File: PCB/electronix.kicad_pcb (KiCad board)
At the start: 2 copper layers, 83.6 x 83.2 mm, 98 parts, among them IC1 ICM-20602, IC2 AP9101CK6-ANTRG1, IC3 DRV8210DRLR, IC4 DRV8210DRLR, J1 USB-C 6pin, J2 PRG, M1 N20 motor, M2 N20 motor, Q1 UMH3N FHA, Q2 757-SSM6N7002KFULF, Q3 757-SSM6N7002KFULF, Q4 Phototransistor, Q5 Phototransistor, Q6 757-SSM6N7002KFULF, Q7 Phototransistor, Q8 Phototransistor, SW1 SW_DIP_x01, SW2 RESET, SW3 START, U1 MCP73213-A6SI/MF, U2 ESP32-WROOM-32, U3 LMR51420YDDRCR

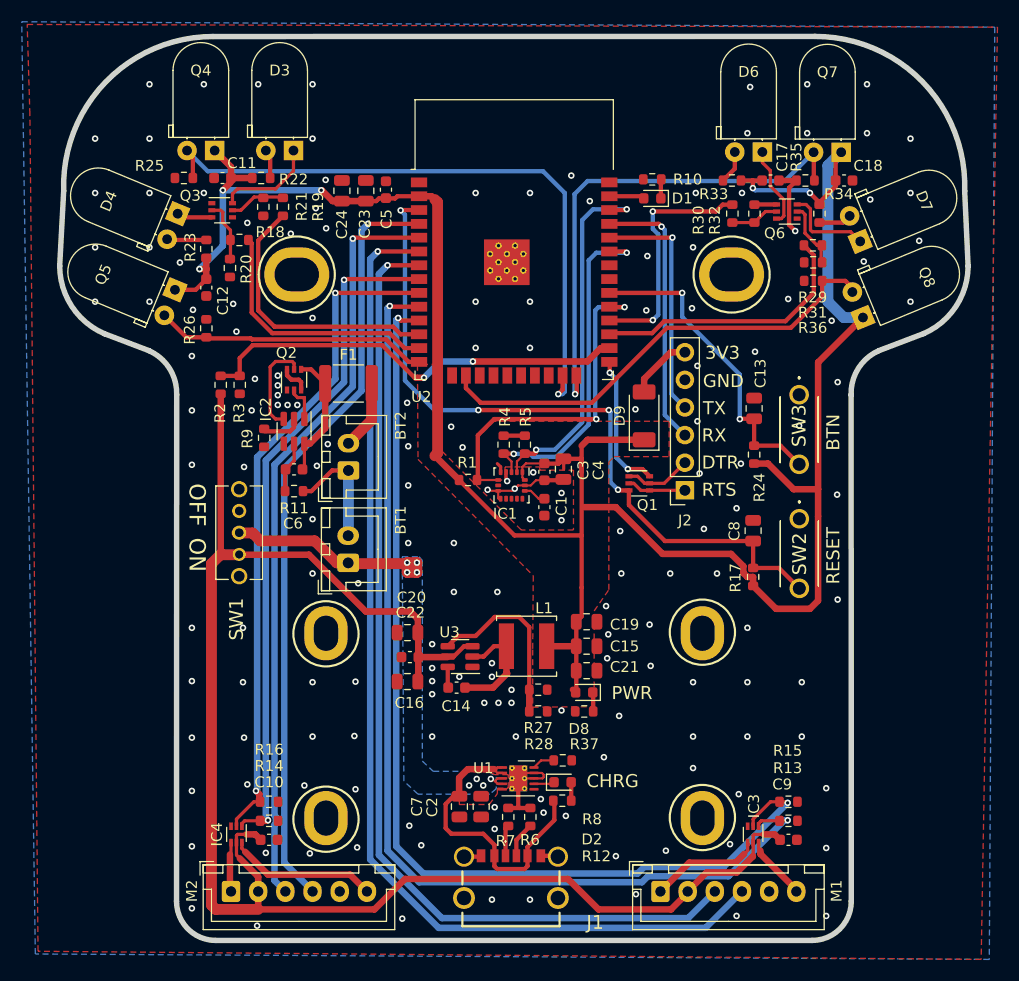
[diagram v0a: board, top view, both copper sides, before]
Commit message: EMI Hardening
Rerouted back layer tracks whereever possible to create a continuous ground plane
Added local vias to all gnd pins
Added via stitching to overhanging areas from the front
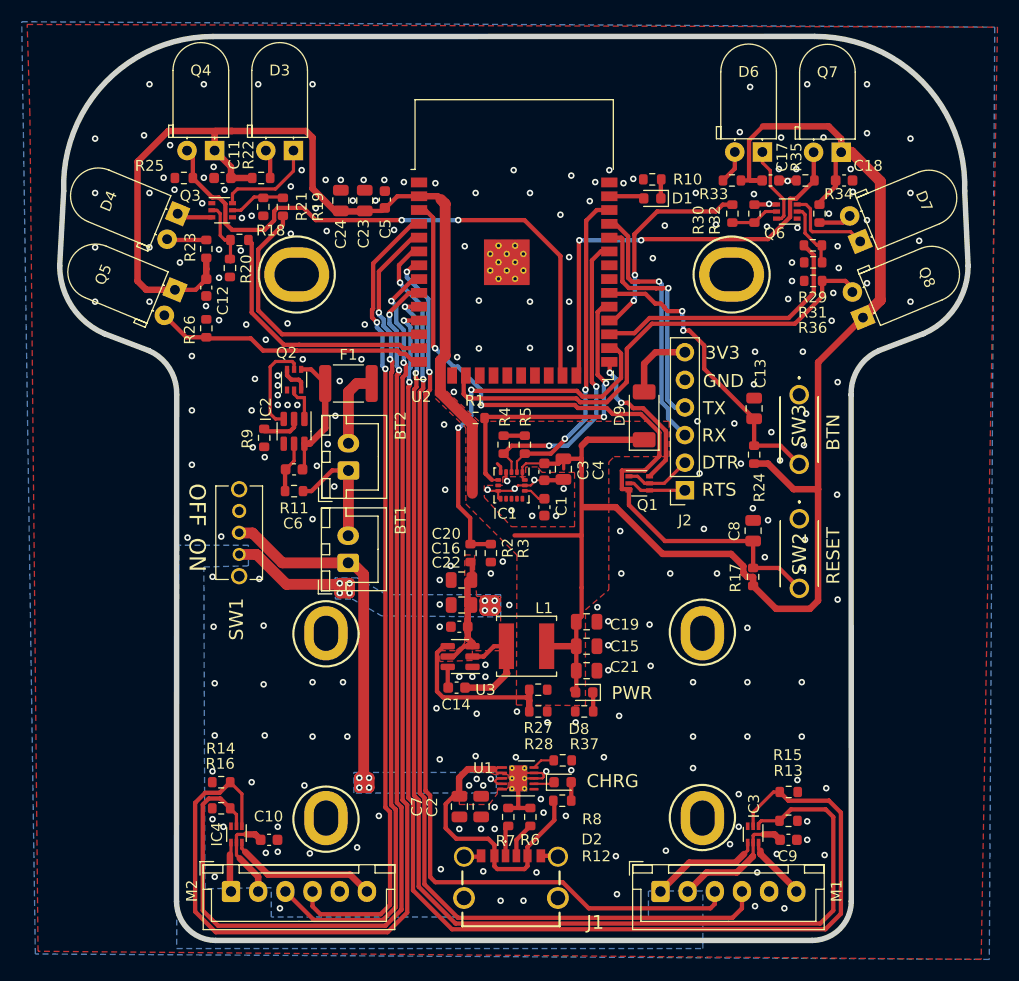
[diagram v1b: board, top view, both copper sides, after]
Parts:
- moved R3 27.8 mm to (128.9, 109.6)
- moved R2 27.7 mm to (127.0, 109.6)
- moved C16 8.62 mm to (126.2, 114.4)
- moved C20 6.94 mm to (126.2, 112.1)
- moved R1 5.74 mm to (127.5, 97.2)
- moved R14 5.65 mm to (104.1, 130.7), turned to 180 degrees
- moved C22 5.33 mm to (126.0, 116.4)
- moved R16 4.44 mm to (104.1, 133.1), turned to 180 degrees
- moved C23 0.91 mm to (117.3, 77.2)
- moved C24 0.91 mm to (115.1, 77.2)
- moved C5 0.91 mm to (119.2, 77.1)
- moved R15 0.90 mm to (156.3, 131.6)
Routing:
- net VCC: track 148.2 -> 49.2 mm, vias 0 -> 8
- net /M2in1: track 62.5 -> 99.5 mm
- net /M2in2: track 61.1 -> 93.2 mm
- net +3V3: track 218.2 -> 242.9 mm, vias 5 -> 0
- net /M1in2: track 94.9 -> 116.0 mm
- net /M1in1: track 96.3 -> 112.0 mm
- net +BATT: track 21.8 -> 36.9 mm
- net /M2c2: track 69.7 -> 76.0 mm, vias 1 -> 2
- net /prox_out_fr: track 46.4 -> 40.0 mm, vias 1 -> 2
- net /prox_out_fl: track 60.0 -> 53.8 mm, vias 1 -> 2
- net /M1c2: track 91.8 -> 86.4 mm, vias 1 -> 2
- net /M1c1: track 98.2 -> 92.9 mm, vias 1 -> 2
- net GND: track 30.2 -> 25.0 mm, vias 170 -> 245
- net /v_sense: track 40.2 -> 35.2 mm
- net /M2c1: track 70.3 -> 74.6 mm, vias 1 -> 2
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- added copper zone on B.Cu, net VCC
- added copper zone on F.Cu, net VCC

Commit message: Add power source switching Add Mouser PN to parts to enable BOM generation Moved PWR indicator to side of board
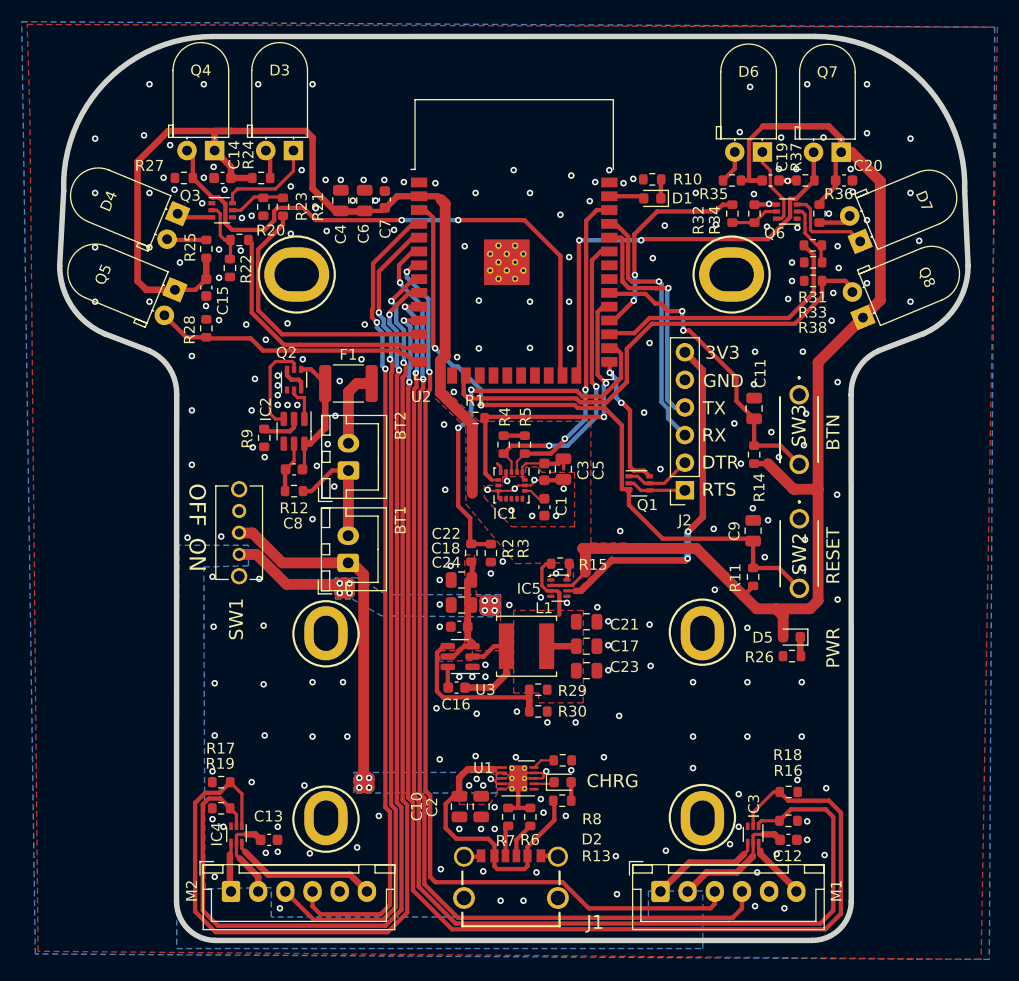
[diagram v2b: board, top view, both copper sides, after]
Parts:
- removed D8: LED, LED_SMD:LED_0603_1608Metric
- removed D9: D, Diode_SMD:D_SOD-128
- removed the R37 at (137.5, 124.2)
- added D5: LED, LED_SMD:LED_0603_1608Metric, F.Cu at (156.6, 117.4)
- added IC5: LM66200DRLR, Package_TO_SOT_SMD:SOT-583-8, F.Cu at (135.2, 112.8)
- added R15: 10k, Resistor_SMD:R_0603_1608Metric, F.Cu at (135.3, 110.6)
- added R26: 330R, Resistor_SMD:R_0603_1608Metric, F.Cu at (156.6, 119.1)
- moved R2 0.08 mm to (127.1, 109.6)
- renumbered C7 to C10, C13 to C11, C9 to C12, C10 to C13, C11 to C14, C12 to C15, C14 to C16, C15 to C17, C16 to C18, C17 to C19, C18 to C20, C19 to C21, C20 to C22, C21 to C23, C22 to C24, C24 to C4, C4 to C5, C23 to C6, C5 to C7, C6 to C8, C8 to C9, R17 to R11, R11 to R12, R12 to R13, R24 to R14, R13 to R16, R14 to R17, R15 to R18, R16 to R19, R18 to R20, R19 to R21, R20 to R22, R21 to R23, R22 to R24, R23 to R25, R25 to R27, R26 to R28, R27 to R29, R28 to R30, R29 to R31, R30 to R32, R31 to R33, R32 to R34, R33 to R35, R34 to R36, R35 to R37, R36 to R38
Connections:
- C17 pad 1: +3V3 -> /3V3_SW
- C21 pad 1: +3V3 -> /3V3_SW
- C23 pad 1: +3V3 -> /3V3_SW
- J2 pad 6: Net-(D9-A) -> /3V3_PRG
- L1 pad 2: +3V3 -> /3V3_SW
- R29 pad 1: +3V3 -> /3V3_SW
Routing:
- net +3V3: track 242.9 -> 209.8 mm
- net /3V3_PRG: track 0.00 -> 32.6 mm, vias 0 -> 2
- net /3V3_SW: track 0.00 -> 9.25 mm
- net Net-(D9-A): track 6.78 -> 0.00 mm
- net /EN: track 68.8 -> 62.8 mm
- net Net-(D5-K): track 0.00 -> 1.71 mm
- net Net-(D8-K): track 1.71 -> 0.00 mm
- net Net-(IC5-ST): track 0.00 -> 1.58 mm
- net /IO0: track 14.2 -> 12.7 mm
- net GND: vias 245 -> 247
- added copper zone on F.Cu, net /3V3_SW

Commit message: Finishing touches shorten ground plane cuts fillet polygon pours add test points and PSU bringup jumper differentiate capacitor footprints by silkscreen
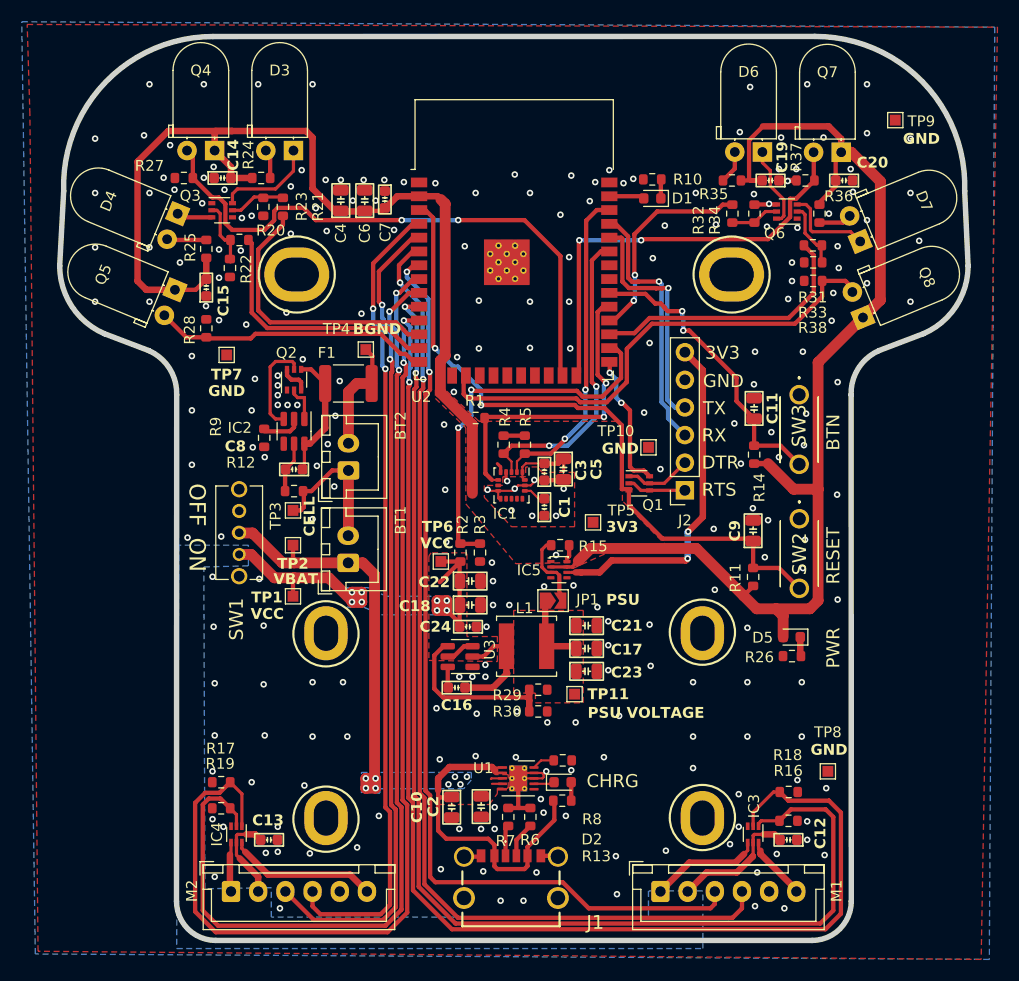
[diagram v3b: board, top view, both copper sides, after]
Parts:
- added JP1: SolderJumper_2_Open, Jumper:SolderJumper-2_P1.3mm_Open_TrianglePad1.0x1.5mm, F.Cu at (134.6, 114.0)
- added TP1: TestPoint, TestPoint:TestPoint_Pad_1.0x1.0mm, F.Cu at (110.7, 113.6)
- added TP10: TestPoint, TestPoint:TestPoint_Pad_1.0x1.0mm, F.Cu at (143.4, 99.9)
- added TP11: TestPoint, TestPoint:TestPoint_Pad_1.0x1.0mm, F.Cu at (136.6, 122.6)
- added TP2: TestPoint, TestPoint:TestPoint_Pad_1.0x1.0mm, F.Cu at (110.7, 108.9)
- added TP3: TestPoint, TestPoint:TestPoint_Pad_1.0x1.0mm, F.Cu at (110.7, 105.7)
- added TP4: TestPoint, TestPoint:TestPoint_Pad_1.0x1.0mm, F.Cu at (117.4, 90.9)
- added TP5: TestPoint, TestPoint:TestPoint_Pad_1.0x1.0mm, F.Cu at (138.3, 106.8)
- added TP6: TestPoint, TestPoint:TestPoint_Pad_1.0x1.0mm, F.Cu at (124.3, 110.4)
- added TP7: TestPoint, TestPoint:TestPoint_Pad_1.0x1.0mm, F.Cu at (104.6, 91.4)
- added TP8: TestPoint, TestPoint:TestPoint_Pad_1.0x1.0mm, F.Cu at (159.9, 129.7)
- added TP9: TestPoint, TestPoint:TestPoint_Pad_1.0x1.0mm, F.Cu at (166.1, 69.8)
- C1, C12, C13, C14, C15, C16, C19, C20, C3, C7, C8: footprint Capacitor_SMD:C_0603_1608Metric -> Custom_parts:C_0603_1608Metric
- C10, C11, C17, C18, C2, C21, C22, C23, C4, C5, C6, C9: footprint Capacitor_SMD:C_0805_2012Metric -> Custom_parts:C_0805_2012Metric
- C24: value 100n/50V -> 100n; footprint Capacitor_SMD:C_0603_1608Metric -> Custom_parts:C_0603_1608Metric
- Q2, Q3, Q6: value 757-SSM6N7002KFULF -> dual NMOS
- SW1: value SW_DIP_x01 -> side slide
- moved IC5 1.70 mm to (135.2, 111.2)
- moved R15 1.70 mm to (135.3, 108.9)
- moved R3 1.00 mm to (127.9, 109.6)
- moved R2 1.00 mm to (126.1, 109.6)
- moved C22 0.81 mm to (127.0, 112.2), turned to 0 degrees
- moved C18 0.80 mm to (127.0, 114.4), turned to 0 degrees
- moved C24 0.80 mm to (126.8, 116.4), turned to 180 degrees
- moved C10 0.71 mm to (125.3, 133.0)
- moved C21 0.36 mm to (137.7, 116.3)
- moved C17 0.21 mm to (137.7, 118.4)
- moved C23 0.06 mm to (137.7, 120.5)
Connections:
- C17 pad 1: /3V3_SW -> /3V3_SW_a
- C21 pad 1: /3V3_SW -> /3V3_SW_a
- C23 pad 1: /3V3_SW -> /3V3_SW_a
- L1 pad 2: /3V3_SW -> /3V3_SW_a
- R29 pad 1: /3V3_SW -> /3V3_SW_a
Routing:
- net VCC: track 49.2 -> 60.2 mm
- net /3V3_SW_a: track 0.00 -> 7.20 mm
- net +BATT: track 36.9 -> 42.4 mm
- net VBUS: track 28.1 -> 32.3 mm
- net Net-(BT2--): track 7.18 -> 10.6 mm
- net Net-(BT1--): track 10.9 -> 13.6 mm
- net /3V3_SW: track 9.25 -> 6.95 mm
- net +3V3: track 209.8 -> 208.4 mm
- net /3V3_PRG: track 32.6 -> 31.5 mm
- net GND: vias 247 -> 243
- added copper zone on F.Cu, net /3V3_SW_a
- removed copper zone on F.Cu, net /3V3_SW
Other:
- board text added: "BGND"
- board text added: "CELL"
- board text added: "PSU"
- board text added: "PSU VOLTAGE"
- board text added: "VBAT"
- board text added: "VCC"

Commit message: ESD hardening
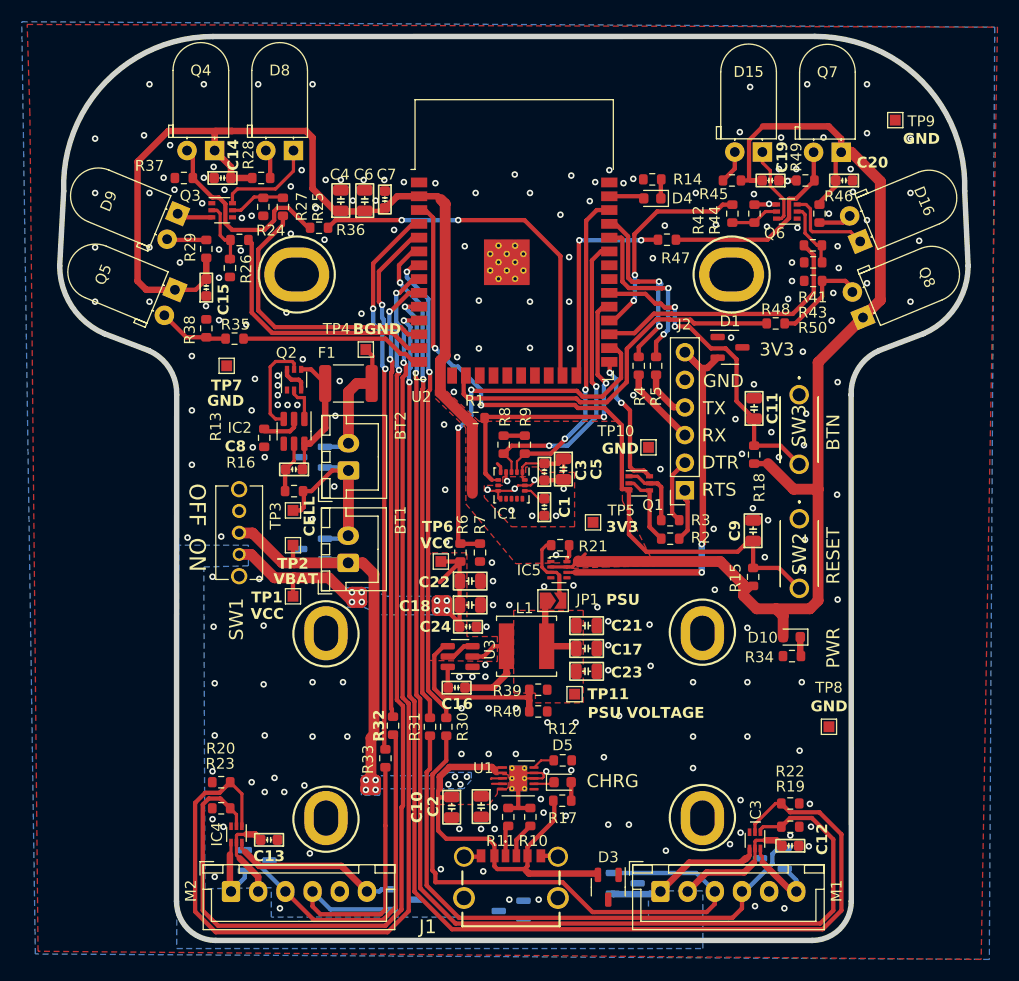
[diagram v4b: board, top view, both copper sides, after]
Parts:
- added D1: PESD5V2S2UT, Package_TO_SOT_SMD:SOT-23-3, F.Cu at (150.9, 90.7)
- added D11: PESD5V2S2UT, Package_TO_SOT_SMD:SOT-23-3, B.Cu at (141.3, 140.0)
- added D12: PESD5V2S2UT, Package_TO_SOT_SMD:SOT-23-3, B.Cu at (154.8, 137.7)
- added D13: PESD5V2S2UT, Package_TO_SOT_SMD:SOT-23-3, B.Cu at (107.4, 137.9)
- added D14: PESD5V2S2UT, Package_TO_SOT_SMD:SOT-23-3, B.Cu at (120.8, 141.5)
- added D2: PESD5V2S2UT, Package_TO_SOT_SMD:SOT-23-3, B.Cu at (130.8, 142.6)
- added D3: PESD5V2S2UT, Package_TO_SOT_SMD:SOT-23-3, F.Cu at (139.7, 140.4)
- added D6: PESD5V2S2UT, Package_TO_SOT_SMD:SOT-23-3, B.Cu at (112.5, 109.2)
- added D7: PESD5V2S2UT, Package_TO_SOT_SMD:SOT-23-3, B.Cu at (112.5, 100.8)
- added R2: 100R, Resistor_SMD:R_0603_1608Metric, F.Cu at (145.4, 108.3)
- added R3: 100R, Resistor_SMD:R_0603_1608Metric, F.Cu at (145.4, 106.6)
- added R30: 100R, Resistor_SMD:R_0603_1608Metric, F.Cu at (124.8, 125.6)
- added R31: 100R, Resistor_SMD:R_0603_1608Metric, F.Cu at (123.3, 125.6)
- added R32: 100R, Resistor_SMD:R_0603_1608Metric, F.Cu at (119.9, 125.5)
- added R33: 100R, Resistor_SMD:R_0603_1608Metric, F.Cu at (119.2, 128.5)
- added R35: 100R, Resistor_SMD:R_0603_1608Metric, F.Cu at (105.3, 89.9)
- added R36: 100R, Resistor_SMD:R_0603_1608Metric, F.Cu at (113.1, 79.7)
- added R4: 100R, Resistor_SMD:R_0603_1608Metric, F.Cu at (142.5, 92.4)
- added R47: 100R, Resistor_SMD:R_0603_1608Metric, F.Cu at (145.1, 80.8)
- added R48: 100R, Resistor_SMD:R_0603_1608Metric, F.Cu at (155.1, 88.5)
- added R5: 100R, Resistor_SMD:R_0603_1608Metric, F.Cu at (144.1, 92.4)
- M1, M2: value N20 motor -> N20
- moved TP8 4.10 mm to (160.0, 125.6)
- moved R22 1.07 mm to (156.4, 132.7)
- moved TP7 1.00 mm to (104.6, 92.4)
- moved C12 0.57 mm to (156.4, 136.5)
- moved IC3 0.57 mm to (153.2, 136.0)
- moved R19 0.57 mm to (156.4, 134.8), turned to 180 degrees
- renumbered D5 to D10, D6 to D15, D7 to D16, D1 to D4, D2 to D5, D3 to D8, D4 to D9, R6 to R10, R7 to R11, R8 to R12, R9 to R13, R10 to R14, R11 to R15, R12 to R16, R13 to R17, R14 to R18, R16 to R19, R17 to R20, R15 to R21, R18 to R22, R19 to R23, R20 to R24, R21 to R25, R22 to R26, R23 to R27, R24 to R28, R25 to R29, R26 to R34, R27 to R37, R28 to R38, R29 to R39, R30 to R40, R31 to R41, R32 to R42, R33 to R43, R34 to R44, R35 to R45, R36 to R46, R37 to R49, R38 to R50, R2 to R6, R3 to R7, R4 to R8, R5 to R9
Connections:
- J2 pad 1: /RTS -> Net-(J2-Pin_1)
- J2 pad 2: /DTR -> Net-(J2-Pin_2)
- J2 pad 3: /RX -> Net-(J2-Pin_3)
- J2 pad 4: /TX -> Net-(J2-Pin_4)
- M1 pad 3: /M1c2 -> Net-(M1-Pin_3)
- M1 pad 4: /M1c1 -> Net-(M1-Pin_4)
- M2 pad 3: /M2c2 -> Net-(M2-Pin_3)
- M2 pad 4: /M2c1 -> Net-(M2-Pin_4)
- Q4 pad 2: /prox_out_fl -> Net-(Q4-E)
- Q5 pad 2: /prox_out_l -> Net-(Q5-E)
- Q7 pad 2: /prox_out_fr -> Net-(Q7-E)
- Q8 pad 2: /prox_out_r -> Net-(Q8-E)
- R19 pad 1: /M1in1 -> GND
- R19 pad 2: GND -> /M1in1
- R37 pad 2: /prox_out_fl -> Net-(Q4-E)
- R38 pad 2: /prox_out_l -> Net-(Q5-E)
- R49 pad 2: /prox_out_fr -> Net-(Q7-E)
- R50 pad 2: /prox_out_r -> Net-(Q8-E)
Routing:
- net Net-(M1-Pin_3): track 0.00 -> 52.5 mm
- net Net-(M1-Pin_4): track 0.00 -> 52.3 mm
- net /M1c1: track 92.9 -> 45.3 mm
- net /M1c2: track 86.4 -> 43.5 mm
- net Net-(M2-Pin_3): track 0.00 -> 33.1 mm
- net /M2c2: track 76.0 -> 46.7 mm
- net Net-(M2-Pin_4): track 0.00 -> 29.2 mm
- net /M2c1: track 74.5 -> 51.0 mm
- net /prox_out_fr: track 39.7 -> 19.6 mm
- net /prox_out_fl: track 53.5 -> 33.8 mm
- net Net-(Q4-E): track 0.00 -> 18.6 mm
- net Net-(Q7-E): track 0.00 -> 18.6 mm
- net /prox_out_r: track 45.1 -> 34.8 mm
- net Net-(Q8-E): track 0.00 -> 8.93 mm
- net /prox_out_l: track 24.9 -> 16.5 mm
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
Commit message: ESD layout edits Add TVS part numbers
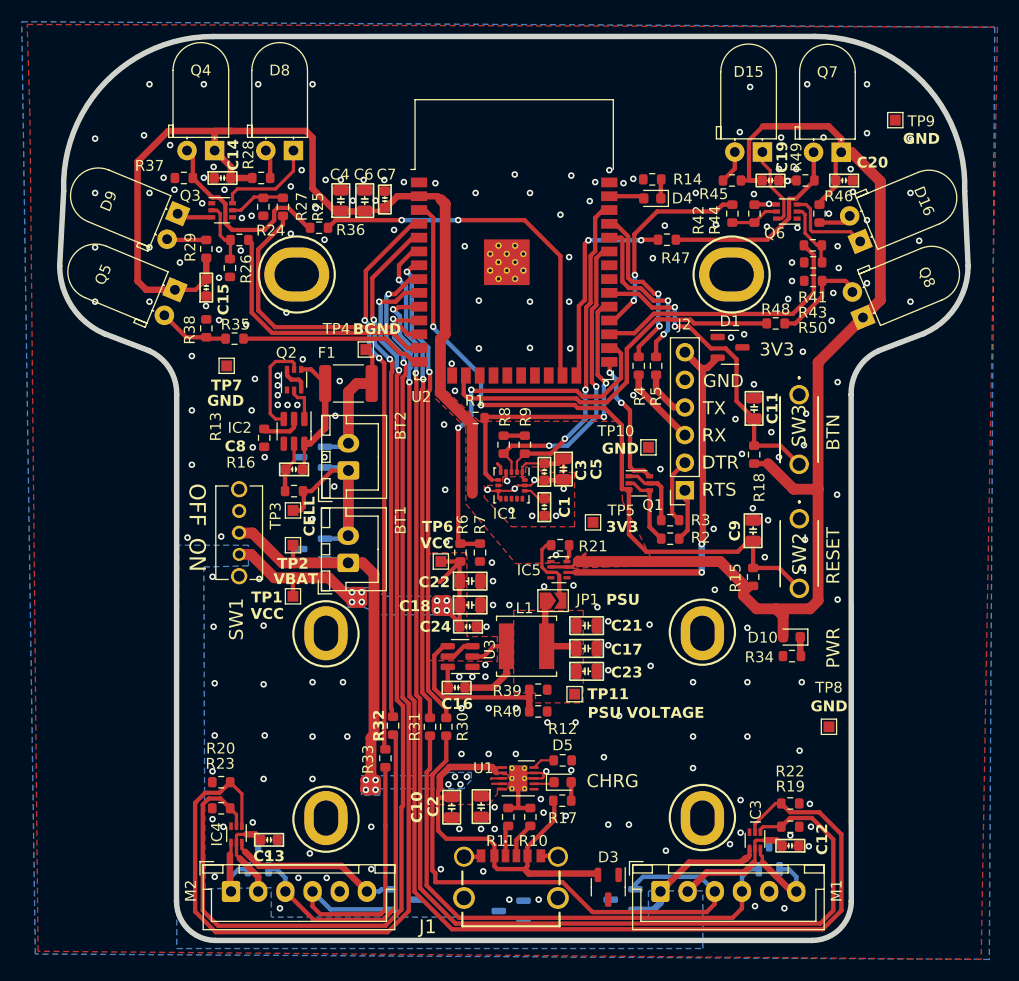
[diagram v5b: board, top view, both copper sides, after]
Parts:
- moved D11 1.51 mm to (141.1, 141.5), turned to 180 degrees
- moved D13 0.35 mm to (107.5, 137.6), turned to 90 degrees
- moved D12 0.33 mm to (154.5, 137.6), turned to 90 degrees
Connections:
- D11 pad 1: /M1p -> Net-(M1-Pin_3)
- D11 pad 2: Net-(M1-Pin_3) -> /M1p
- D12 pad 1: Net-(M1-Pin_4) -> /M1n
- D12 pad 2: /M1n -> Net-(M1-Pin_4)
- D13 pad 1: /M2p -> Net-(M2-Pin_3)
- D13 pad 2: Net-(M2-Pin_3) -> /M2p
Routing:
- net Net-(M1-Pin_4): track 52.3 -> 49.3 mm
- net Net-(M2-Pin_3): track 33.1 -> 30.8 mm
- net /M2in2: track 93.4 -> 95.3 mm
- net /M1in2: track 113.5 -> 115.1 mm
- net Net-(M1-Pin_3): track 52.5 -> 51.0 mm
- net /M1in1: track 110.0 -> 111.4 mm
- net /RX: track 17.2 -> 16.0 mm
- net /M2in1: track 99.4 -> 100.5 mm
- net /M1p: track 14.7 -> 13.8 mm
- net /TX: track 16.6 -> 15.7 mm
- net /M2p: track 6.72 -> 7.49 mm
- net /M1n: track 8.08 -> 8.73 mm
- net /M2c1: track 51.0 -> 51.5 mm
- net GND: vias 234 -> 238
